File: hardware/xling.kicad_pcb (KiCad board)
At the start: 2 copper layers, 45 x 60 mm, 54 parts, among them J3 MCP73831, J4 USB_OTG, J5 AVR ISP, J6 Battery, Q1 TP0610T, SW2 Up, SW3 Select, SW4 Down, U1 LT1109CZ-12, U2 ATMEGA328P-AU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

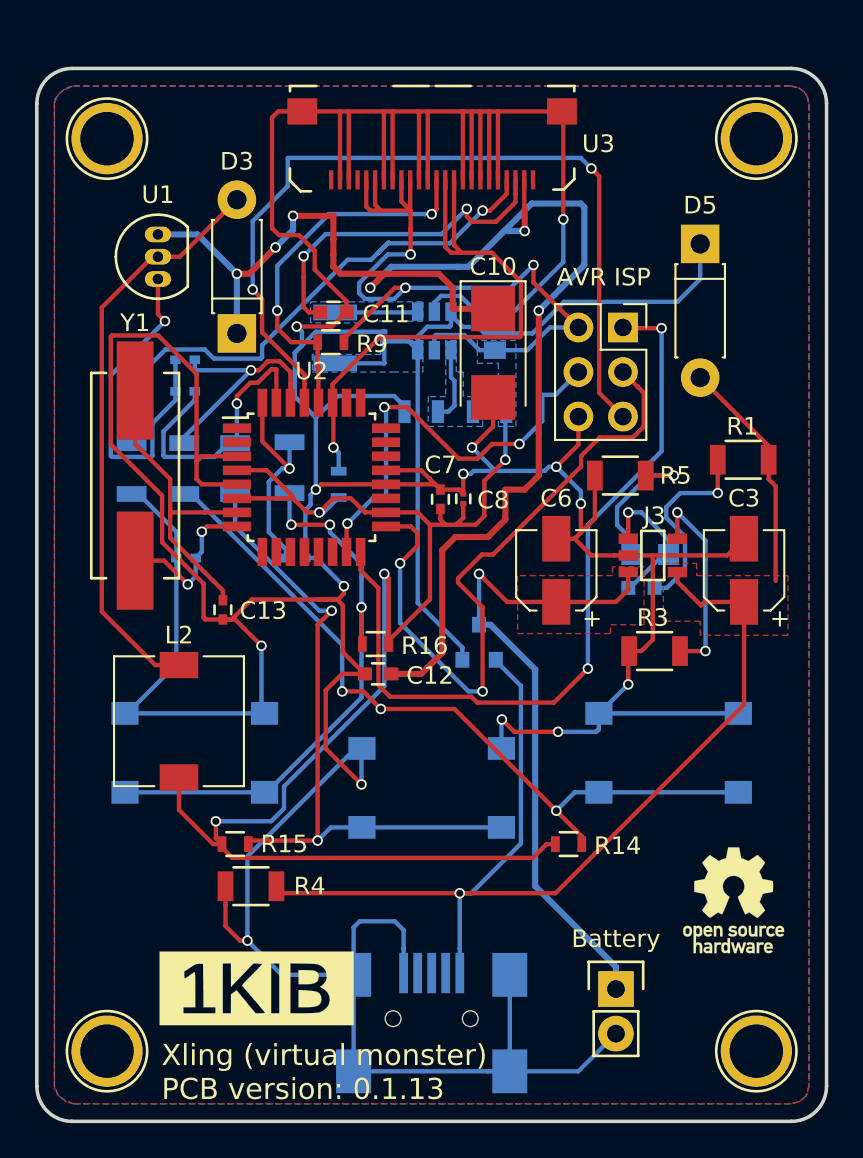
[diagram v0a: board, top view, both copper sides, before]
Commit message: patch 0.1.17: Add 3.3V linear regulator for USB mode.
- Fix placement of U1 (mirrored);
- Fix placement of the AVR ISR connector;
- Adjust U3 pads to easy soldering (they are a bit bigger now);
- Add marks for D1 and D2 LEDs;
- Replace models of several components to be in 0805 or 0603 cases;
- Add fixed linear 3.3V voltage regulator for USB mode;
- Re-route PCB according to the all of these changes.

Signed-off-by: Dmitry Salychev <darkness.bsd@gmail.com>
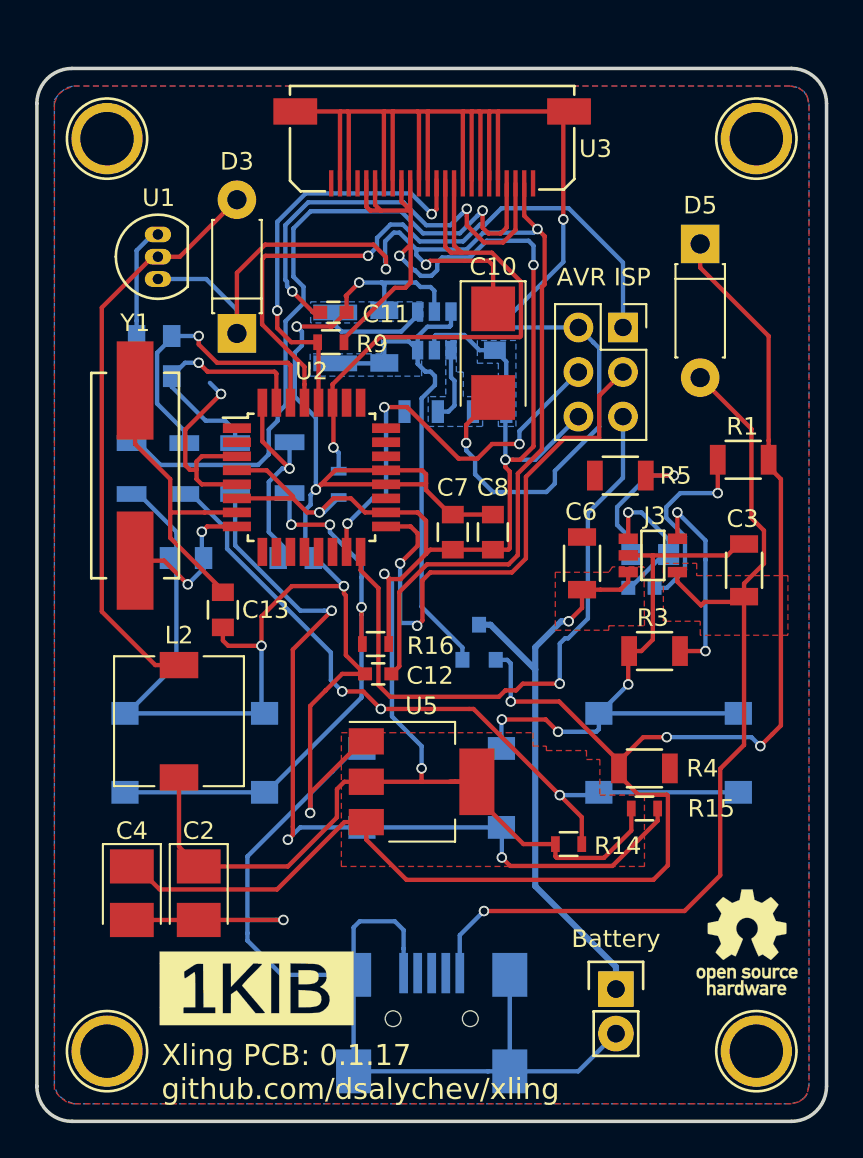
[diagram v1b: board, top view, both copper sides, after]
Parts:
- added C2: 10uF, Capacitors_Tantalum_SMD:CP_Tantalum_Case-B_EIA-3528-21_Reflow, F.Cu at (128.2, 125.0)
- added C4: 10uF, Capacitors_Tantalum_SMD:CP_Tantalum_Case-B_EIA-3528-21_Reflow, F.Cu at (124.4, 125.0)
- added U5: LM1117-3.3, TO_SOT_Packages_SMD:SOT-223-3Lead_TabPin2, F.Cu at (140.9, 118.6)
- C13, C15, C18, C19, C20, C7: footprint Capacitors_SMD:C_0402 -> Capacitors_SMD:C_0805
- C3, C6: footprint Capacitors_SMD:CP_Elec_4x5.3 -> Capacitors_SMD:C_1206
- C5: footprint Capacitors_SMD:C_0201 -> Capacitors_SMD:C_1206
- C8: footprint Capacitors_SMD:C_0201 -> Capacitors_SMD:C_0805
- U1: footprint TO_SOT_Packages_THT:TO-92_Inline_Narrow_Oval -> Xling Footprints:TO-92_LT1109CZ
- moved R15 23.4 mm to (153.6, 120.2)
- moved R4 23.4 mm to (153.6, 117.9), turned to 0 degrees
- moved C8 2.54 mm to (145.0, 104.4)
- moved REF*** 2.51 mm to (159.5, 127.8)
- moved C18 2.22 mm to (125.7, 93.2)
- moved C7 2.00 mm to (142.7, 104.4)
- moved C19 1.97 mm to (125.7, 95.5)
- moved C6 1.52 mm to (150.1, 106.2)
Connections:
- D5 pad 1: Net-(C5-Pad1) -> Net-(C4-Pad1)
- J5 pad 1: /ISP_PDO_MISO -> /ISP_RST
- J5 pad 2: +3V3 -> GND
- J5 pad 5: /ISP_RST -> /ISP_PDO_MISO
- J5 pad 6: GND -> +3V3
- Q1 pad 1: Net-(C3-Pad1) -> Net-(C4-Pad1)
- R1 pad 1: Net-(C3-Pad1) -> Net-(C4-Pad1)
- R4 pad 1: Net-(C3-Pad1) -> Net-(C4-Pad1)
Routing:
- net Net-(C4-Pad1): track 0.00 -> 94.6 mm, vias 0 -> 3
- net GND: track 368.6 -> 328.7 mm, vias 15 -> 13
- net Net-(C3-Pad1): track 75.7 -> 54.0 mm
- net Net-(C5-Pad1): track 46.7 -> 29.6 mm
- net +3V3: track 134.9 -> 149.3 mm, vias 7 -> 6
- net Net-(R15-Pad2): track 37.6 -> 49.3 mm, vias 2 -> 3
- net /ISP_RST: track 48.4 -> 37.1 mm, vias 2 -> 1
- net +12V: track 84.2 -> 74.3 mm, vias 6 -> 3
- net /ISP_PDO_MISO: track 44.5 -> 35.7 mm, vias 2 -> 1
- net Net-(R2-Pad2): track 31.8 -> 39.9 mm
- net /ISP_SCK: track 38.9 -> 31.7 mm
- net Net-(C11-Pad1): track 19.5 -> 24.9 mm
- net Net-(C6-Pad1): track 37.7 -> 33.6 mm
- net /BTN1: track 13.9 -> 17.0 mm
- net /OLED_SCL: track 21.9 -> 24.3 mm
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- added copper zone on F.Cu, net +3V3
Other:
- board text added: "Xling PCB: 0.1.17 github.com/dsalychev/xling"
- board text removed: "Xling (virtual monster) PCB version: 0.1.13"

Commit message: patch 0.1.18: Add new KiCad modules and scheme changes.
Signed-off-by: Dmitry Salychev <darkness.bsd@gmail.com>
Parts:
- removed C12: 2.2uF, Capacitors_SMD:C_0603
- removed D1: charging, LEDs:LED_0603
- removed D2: charged, LEDs:LED_0805
- removed the G*** at (131.5, 130.4)
- removed the REF** at (160.0, 134.0)
- removed the REF** at (123.0, 134.0)
- removed the REF** at (160.0, 82.0)
- removed the REF** at (123.0, 82.0)
- removed REF***: OSHW-Logo_5.7x6mm_SilkScreen, Symbols:OSHW-Logo_5.7x6mm_SilkScreen
- added C9: 1pF, Capacitors_SMD:C_0805, F.Cu at (148.3, 99.6)
- added G***: LOGO, Xling Footprints:terterm, B.Cu at (145.5, 86.4)
- added G***: LOGO, Xling Footprints:oshw, F.Cu at (147.1, 81.3)
- added Q2: NTR0202PL, TO_SOT_Packages_SMD:SOT-23, F.Cu at (142.7, 99.8)
- added Q3: NTA4153N, SC-75_SOT-416, F.Cu at (139.7, 99.6)
- added R10: 100K, Resistors_SMD:R_1206, F.Cu at (131.1, 105.4)
- added REF**: MountingHole_2.2mm_M2_Pad_Via, Mounting_Holes:MountingHole_2.2mm_M2_Pad_Via, F.Cu at (125.7, 80.0)
- added REF**: MountingHole_2.2mm_M2_Pad_Via, Mounting_Holes:MountingHole_2.2mm_M2_Pad_Via, F.Cu at (153.7, 80.0)
- C11, L2, U2: moved to B.Cu
- C15, C18, C19, C20, J4, R17, R18, R19, R8: moved to F.Cu
- J6: footprint Pin_Headers:Pin_Header_Straight_1x02 -> Xling Footprints:Pin_Header_Straight_1x02
- R1: value 470R -> 100K; moved to B.Cu
- R5: value 470R -> 100K
- U5: footprint TO_SOT_Packages_SMD:SOT-223-3Lead_TabPin2 -> Xling Footprints:SOT-223-3Lead_TabPin2; moved to B.Cu
- Y1: footprint Crystals:Crystal_HC49-SD_SMD -> Xling Footprints:Crystal_HC49-SD_SMD
- moved L1 32.2 mm to (152.1, 121.2)
- moved D5 31.4 mm to (125.5, 86.6)
- moved L2 27.7 mm to (152.0, 103.1), turned to 0 degrees
- moved R6 27.5 mm to (126.0, 117.6), turned to 270 degrees
- moved U4 26.8 mm to (131.2, 117.6), turned to 180 degrees
- moved SW2 26.7 mm to (128.8, 111.8)
- moved C5 26.6 mm to (128.0, 117.6), turned to 270 degrees
- moved R1 26.3 mm to (133.9, 93.5), turned to 270 degrees
- moved R7 26.3 mm to (124.0, 117.6), turned to 90 degrees
- moved U1 25.3 mm to (151.1, 88.4), turned to 0 degrees
- moved C18 25.2 mm to (144.0, 110.5), turned to 270 degrees
- moved C19 25.1 mm to (145.8, 110.5), turned to 270 degrees
- moved R14 23.5 mm to (131.1, 107.4), turned to 180 degrees
- moved SW4 23.2 mm to (150.6, 111.8)
- moved R15 22.9 mm to (132.8, 110.5), turned to 270 degrees
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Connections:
- J3 pad 1: Net-(D1-Pad1) -> /BAT_STAT
- J4 pad 2: Net-(J4-Pad2) -> (no net)
- J4 pad 3: Net-(J4-Pad3) -> (no net)
- J4 pad 4: Net-(J4-Pad4) -> (no net)
- R1 pad 1: Net-(C4-Pad1) -> +3V3
- R1 pad 2: Net-(D1-Pad2) -> /OLED_RES
- R5 pad 1: GND -> +12V
- U2 pad 1: Net-(U2-Pad1) -> /OLED_RES
- U2 pad 10: Net-(U2-Pad10) -> (no net)
- U2 pad 11: Net-(U2-Pad11) -> (no net)
- U2 pad 12: Net-(U2-Pad12) -> (no net)
- U2 pad 13: Net-(U2-Pad13) -> (no net)
- U2 pad 14: Net-(U2-Pad14) -> (no net)
- U2 pad 19: Net-(U2-Pad19) -> (no net)
- U2 pad 2: Net-(U2-Pad2) -> /OLED_PWR
- U2 pad 22: Net-(U2-Pad22) -> (no net)
- U2 pad 23: Net-(U2-Pad23) -> (no net)
- U2 pad 24: Net-(U2-Pad24) -> (no net)
- U2 pad 25: Net-(U2-Pad25) -> (no net)
- U2 pad 26: Net-(U2-Pad26) -> (no net)
- U2 pad 9: Net-(U2-Pad9) -> /BAT_STAT
- U3 pad 1: Net-(U3-Pad1) -> (no net)
- U3 pad 23: +12V -> /OLED_VCC
- U3 pad 24: Net-(U3-Pad24) -> (no net)
- U3 pad 4: Net-(U3-Pad4) -> (no net)
- U3 pad 9: +3V3 -> /OLED_RES
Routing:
- net GND: track 328.7 -> 220.6 mm, vias 13 -> 9
- net Net-(R15-Pad2): track 49.3 -> 18.7 mm, vias 3 -> 1
- net /BAT_STAT: track 0.00 -> 30.5 mm, vias 0 -> 1
- net Net-(R2-Pad2): track 39.9 -> 11.3 mm
- net /ISP_PDO_MISO: track 35.7 -> 10.0 mm, vias 1 -> 0
- net /ISP_SCK: track 31.7 -> 8.35 mm, vias 2 -> 0
- net Net-(C4-Pad1): track 94.6 -> 72.3 mm, vias 3 -> 4
- net /OLED_RES: track 0.00 -> 20.4 mm, vias 0 -> 1
- net /ISP_RST: track 37.1 -> 18.1 mm, vias 1 -> 2
- net Net-(R14-Pad2): track 43.6 -> 25.3 mm, vias 3 -> 1
- net +12V: track 74.3 -> 56.1 mm, vias 3 -> 0
- net Net-(C11-Pad1): track 24.9 -> 7.74 mm, vias 2 -> 1
- net Net-(L1-Pad2): track 6.25 -> 22.3 mm
- net Net-(C6-Pad1): track 33.6 -> 20.2 mm, vias 1 -> 0
- net /OLED_VCC: track 0.00 -> 12.6 mm
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- removed copper zone on B.Cu, net +3V3
- removed copper zone on F.Cu, net +3V3
- removed copper zone on F.Cu, net Net-(C3-Pad1)
- removed copper zone on B.Cu, net Net-(C5-Pad1)
- removed copper zone on F.Cu, net Net-(C6-Pad1)
- removed copper zone on B.Cu, net Net-(L1-Pad2)
- removed copper zone on B.Cu, net Net-(R6-Pad2)
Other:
- board size 45 x 60 mm -> 35.6 x 48.3 mm
- board text added: "Xling PCB ver: 0.1.18"
- board text added: "terterm.com"
- board text removed: "AVR ISP"
- board text removed: "Battery"
- board text removed: "Down"
- board text removed: "Select"
- board text removed: "Up"
- board text removed: "Xling PCB: 0.1.17 github.com/dsalychev/xling"
- board text removed: "charged"
- board text removed: "charging"

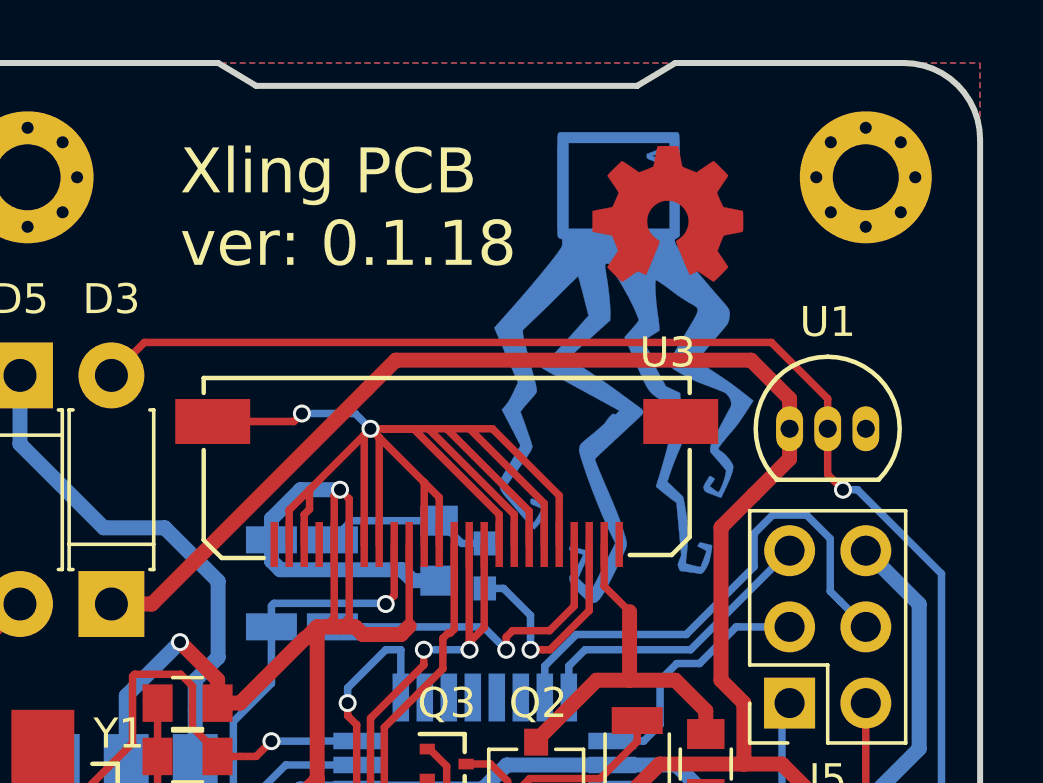
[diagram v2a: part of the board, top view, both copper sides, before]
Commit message: patch 0.1.20: Update PCB and prepare gerber files for production.
Signed-off-by: Dmitry Salychev <darkness.bsd@gmail.com>
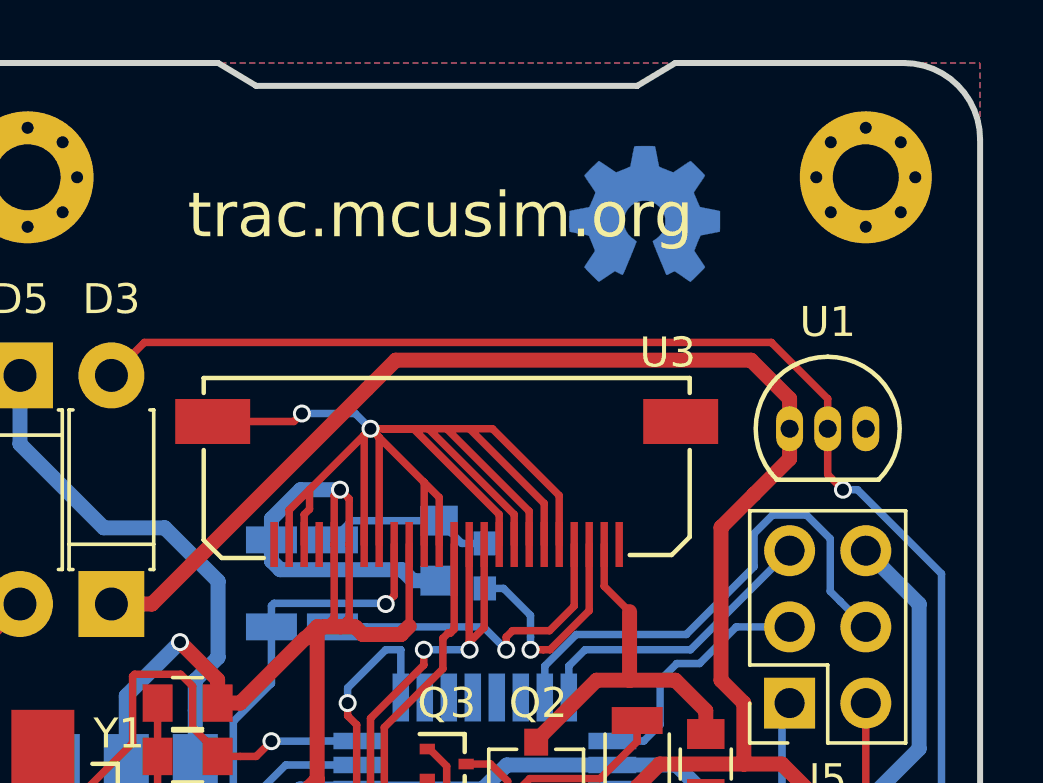
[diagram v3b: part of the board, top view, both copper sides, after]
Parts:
- removed the G*** at (145.5, 86.4)
- G***: moved to B.Cu
- moved G*** 0.76 mm to (146.3, 81.3), turned to 180 degrees
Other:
- board text added: "Xling PCB ver: 0.1.20"
- board text added: "trac.mcusim.org"
- board text removed: "Xling PCB ver: 0.1.18"
- board text removed: "terterm.com"

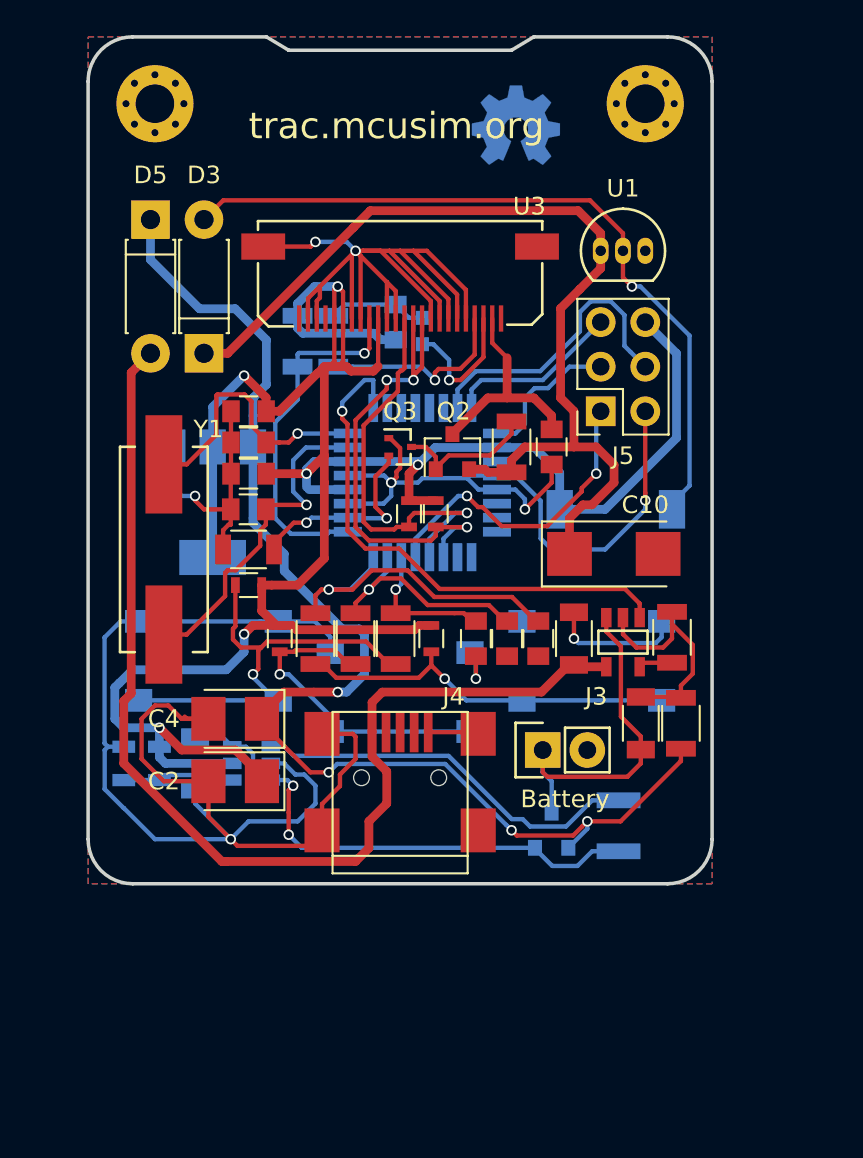
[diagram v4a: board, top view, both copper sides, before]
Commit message: patch 0.1.22: Power supply scheme modified and PCB update.
Signed-off-by: Dmitry Salychev <darkness.bsd@gmail.com>
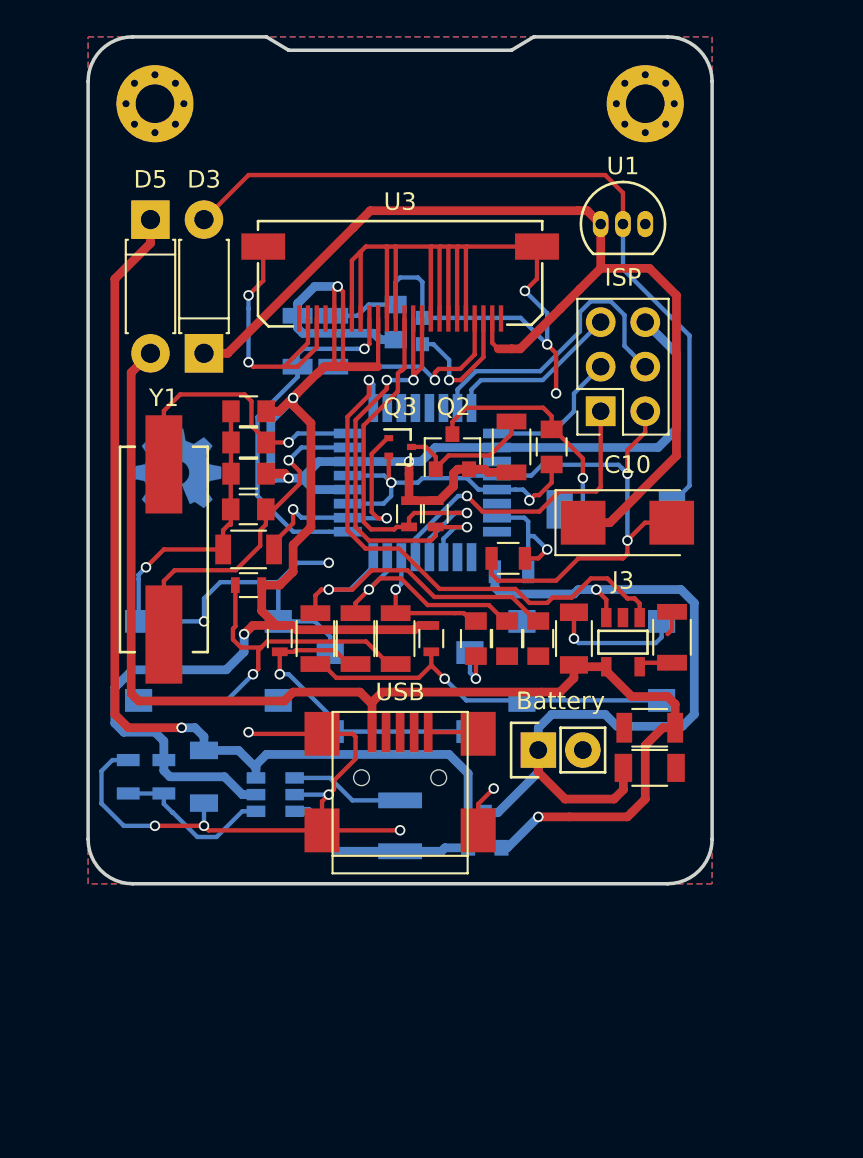
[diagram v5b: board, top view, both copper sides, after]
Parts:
- removed C2, C4: 10uF, Capacitors_Tantalum_SMD:CP_Tantalum_Case-B_EIA-3528-21_Reflow
- removed the G*** at (146.3, 81.3)
- removed U5: LM1117-3.3, Xling Footprints:SOT-223-3Lead_TabPin2
- added G***: LOGO, lib_fp:oshw, B.Cu at (127.0, 100.8)
- added R11: 191K, Resistors_SMD:R_0805, B.Cu at (146.1, 106.7)
- added R12: 110K, Resistors_SMD:R_0805, F.Cu at (145.9, 105.9)
- Q1: value TP0610T -> NTR0202PL
- Q3: footprint SC-75_SOT-416 -> Xling Footprints:SC-75_SOT-416
- R3: value 2K2 -> 2K7
- moved L1 12.4 mm to (139.7, 121.2)
- moved Q1 3.81 mm to (144.5, 121.4)
- moved C6 2.59 mm to (153.9, 117.9), turned to 0 degrees
- moved U4 2.23 mm to (132.6, 119.4)
- moved C10 1.94 mm to (152.7, 103.9)
- moved R4 1.80 mm to (153.9, 115.6), turned to 180 degrees
- moved U1 1.52 mm to (151.1, 86.9)
- moved C5 0.92 mm to (128.5, 118.4)
- moved R6 0.80 mm to (126.2, 118.4)
- moved R7 0.80 mm to (124.2, 118.4)
- moved J6 0.25 mm to (147.6, 116.8)
- renumbered J5 to ISP, J4 to USB
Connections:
- D5 pad 1: Net-(C4-Pad1) -> Net-(C5-Pad1)
- L2 pad 1: +3V3 -> /OLED_VCC
- Q1 pad 1: Net-(C4-Pad1) -> Net-(C3-Pad1)
- Q2 pad 2: +12V -> +3V3
- Q3 pad 1: GND -> /OLED_PWR
- Q3 pad 2: /OLED_PWR -> GND
- R4 pad 1: Net-(C4-Pad1) -> Net-(C3-Pad1)
- R5 pad 1: +12V -> +3V3
- U2 pad 23: (no net) -> /BAT_LVL
- U3 pad 23: /OLED_VCC -> +12V
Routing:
- net Net-(C4-Pad1): track 72.3 -> 0.00 mm, vias 4 -> 0
- net Net-(C5-Pad1): track 30.3 -> 67.9 mm, vias 2 -> 1
- net Net-(C6-Pad1): track 20.2 -> 45.5 mm, vias 0 -> 1
- net Net-(L1-Pad2): track 22.3 -> 6.54 mm
- net +3V3: track 144.3 -> 128.6 mm, vias 6 -> 5
- net GND: track 220.6 -> 229.6 mm, vias 9 -> 20
- net /BAT_LVL: track 0.00 -> 7.97 mm, vias 0 -> 1
- net Net-(C3-Pad1): track 63.9 -> 71.4 mm, vias 0 -> 1
- net +12V: track 56.1 -> 59.4 mm
- net Net-(R6-Pad2): track 6.51 -> 9.27 mm
- net Net-(D3-Pad2): track 43.1 -> 45.7 mm, vias 1 -> 0
- net /OLED_PWR: track 11.6 -> 14.0 mm
- net /OLED_VCC: track 12.6 -> 14.2 mm, vias 0 -> 1
- net /BAT_STAT: track 30.5 -> 31.1 mm
- net Net-(R14-Pad2): track 25.3 -> 25.9 mm
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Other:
- board text added: "(mcusim.org)"
- board text added: "0.1.22"
- board text added: "Xling Virtual Monster by MCUSim"
- board text removed: "Xling PCB ver: 0.1.20"
- board text removed: "trac.mcusim.org"
